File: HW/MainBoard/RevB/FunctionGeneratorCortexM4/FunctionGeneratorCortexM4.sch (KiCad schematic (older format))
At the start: 2 parts, among them J1 Conn_02x05_Odd_Even, J2 Screw_Terminal_01x02

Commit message: REVB Update
- Changed TRIGIN J5 header to 2.54mm
- Changed IO J1 header to 2x05
- Added second charge pump IC
- Changed analog output circuit
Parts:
- J1: footprint Connector_IDC:IDC-Header_2x06_P2.54mm_Vertical -> Connector_IDC:IDC-Header_2x05_P2.54mm_Vertical
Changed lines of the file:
@@
 F 0 "J1" H 9025 5917 50  0000 C CNN
 F 1 "Conn_02x05_Odd_Even" H 9025 5826 50  0000 C CNN
-F 2 "Connector_IDC:IDC-Header_2x06_P2.54mm_Vertical" H 8975 5500 50  0001 C CNN
+F 2 "Connector_IDC:IDC-Header_2x05_P2.54mm_Vertical" H 8975 5500 50  0001 C CNN
 F 3 "~" H 8975 5500 50  0001 C CNN
 	1    8975 5500

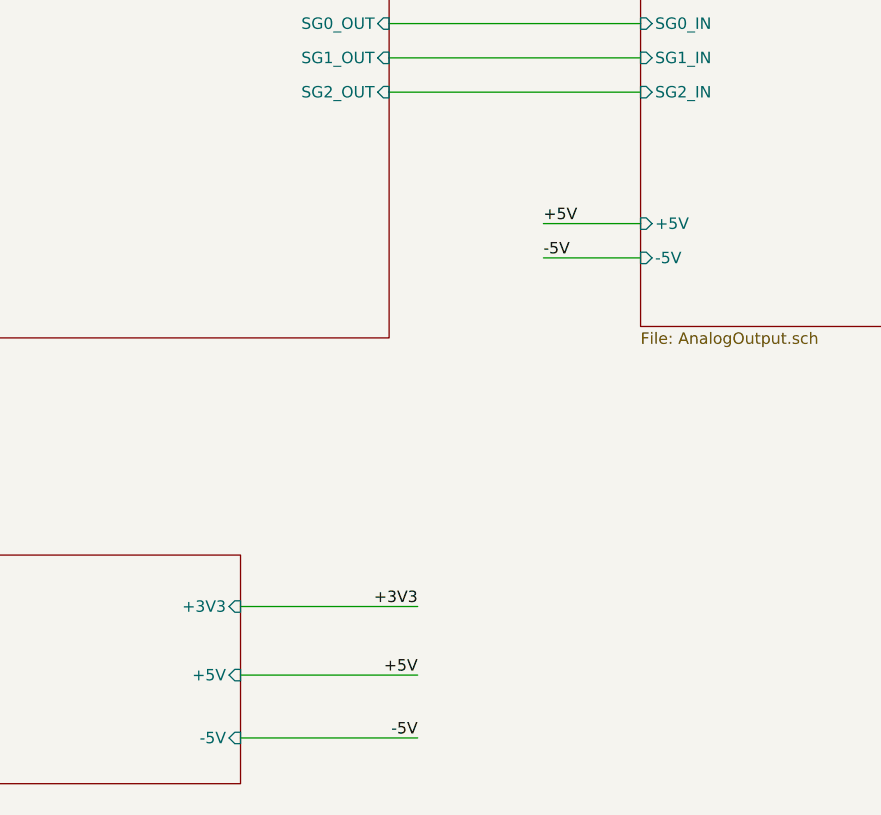
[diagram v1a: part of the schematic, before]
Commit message: Modified PowerSupply section
- Added +2.5V ref
- Added Vin->5V LDO
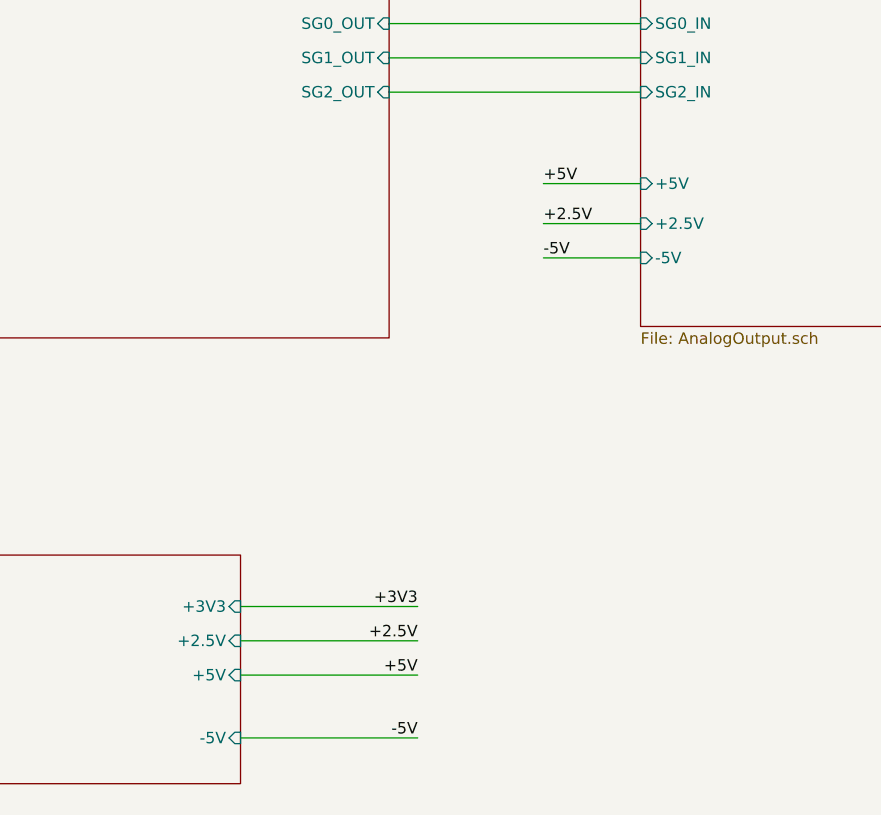
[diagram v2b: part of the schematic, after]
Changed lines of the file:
@@
 F4 "+3V3" I R 4900 5425 50
 F5 "-5V" I R 4900 6000 50
+F6 "+2.5V" I R 4900 5575 50
 $EndSheet
 $Comp
@@
 F9 "SG1_IN" I L 6650 3025 50
 F10 "SG2_IN" I L 6650 3175 50
-F11 "+5V" I L 6650 3750 50
+F11 "+5V" I L 6650 3575 50
 F12 "-5V" I L 6650 3900 50
+F13 "+2.5V" I L 6650 3750 50
 $EndSheet
 Wire Wire Line
@@
 IDC RIBBON CABLE\nTO BNC COAX FRONT PANEL
 Wire Wire Line
-	6650 3750 6225 3750
-Text Label 6225 3750 0    50   ~ 0
+	6650 3575 6225 3575
+Text Label 6225 3575 0    50   ~ 0
 +5V
 Wire Wire Line
 	3350 3950 3025 3950
+Wire Wire Line
+	6225 3750 6650 3750
+Text Label 6225 3750 0    50   ~ 0
++2.5V
+Wire Wire Line
+	4900 5575 5675 5575
+Text Label 5675 5575 2    50   ~ 0
++2.5V
 $EndSCHEMATC

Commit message: OPTIMIZED REVB LAYOUT
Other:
- moved on the sheet: J1, J2
